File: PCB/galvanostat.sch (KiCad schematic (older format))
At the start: 27 parts, among them J0 Conn_01x02, J1 Conn_01x02, J2 Conn_01x02, U1 L7815, U2 LM358, U3 LM358, U4 LMC7660, U5 INA105KP, U6 LM358

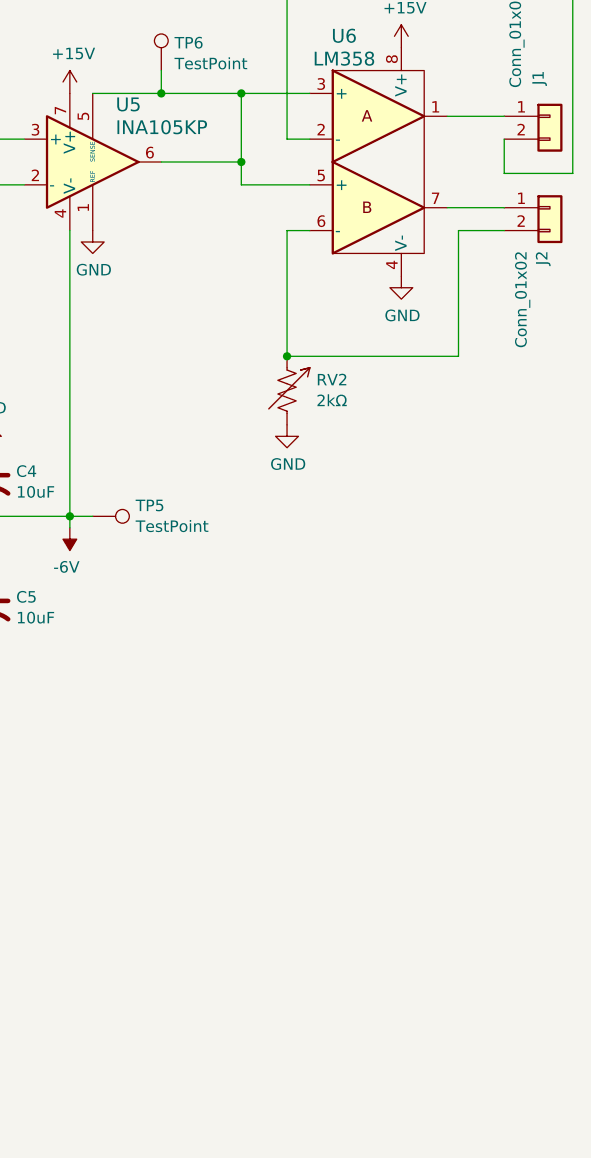
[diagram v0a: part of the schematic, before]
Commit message: dual to quad
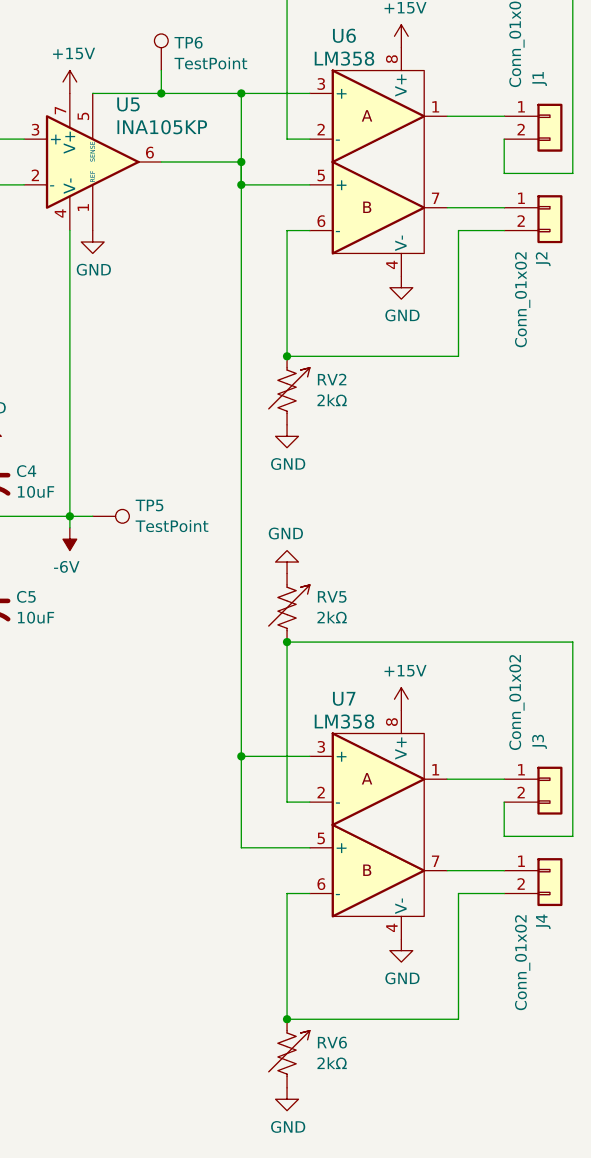
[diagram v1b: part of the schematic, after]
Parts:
- added J3, J4: Conn_01x02, Connector_Molex:Molex_KK-254_AE-6410-02A_1x02_P2.54mm_Vertical, symbol Connector_Generic:Conn_01x02
- added RV5, RV6: 2kΩ, Potentiometer_THT:Potentiometer_Bourns_3299W_Vertical, symbol Device:R_Variable_US
- added U7: LM358, Package_DIP:DIP-8_W7.62mm_Socket_LongPads, symbol LM358:LM358
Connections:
- net +15V: now also U7.8 (V+)
- net GND: now also RV5.1, RV6.2, U7.4 (V-)
- net at TP6.1, U5.5 (SENSE), U5.6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: now also U7.3 (+), U7.5 (+)
- new net: J3.1 (Pin_1), U7.1
- new net: J3.2 (Pin_2), RV5.2, U7.2 (-)
- new net: J4.1 (Pin_1), U7.7
- new net: J4.2 (Pin_2), RV6.1, U7.6 (-)
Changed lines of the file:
@@
 EESchema Schematic File Version 4
 LIBS:galvanostat-cache
-EELAYER 26 0
+EELAYER 29 0
 EELAYER END
 $Descr USLetter 11000 8500
 encoding utf-8
 Sheet 1 1
-Title "Dual Galvanostat"
-Date "2018-11-14"
-Rev "B"
+Title "Galvanostat"
+Date "2019-06-11"
+Rev "C"
 Comp ""
 Comment1 ""
@@
 Entry Wire Line
 	2700 3950 2800 4050
+$Comp
+L Connector_Generic:Conn_01x02 J3
+U 1 1 5D00B8A6
+P 9050 5150
+F 0 "J3" V 9000 5350 50  0000 R CNN
+F 1 "Conn_01x02" V 8900 5700 50  0000 R CNN
+F 2 "Connector_Molex:Molex_KK-254_AE-6410-02A_1x02_P2.54mm_Vertical" H 9050 5150 50  0001 C CNN
+F 3 "" H 9050 5150 50  0001 C CNN
+	1    9050 5150
+	1    0    0    -1
+$EndComp
+$Comp
+L power:+15V #PWR03
+U 1 1 5D00B8AC
+P 8400 4850
+F 0 "#PWR03" H 8400 4700 50  0001 C CNN
+F 1 "+15V" H 8415 5023 50  0000 C CNN
+F 2 "" H 8400 4850 50  0001 C CNN
+F 3 "" H 8400 4850 50  0001 C CNN
+	1    8400 4850
+	1    0    0    -1
+$EndComp
+$Comp
+L power:GND #PWR01
+U 1 1 5D00B8B2
+P 7900 4250
+F 0 "#PWR01" H 7900 4000 50  0001 C CNN
+F 1 "GND" H 7905 4077 50  0000 C CNN
+F 2 "" H 7900 4250 50  0001 C CNN
+F 3 "" H 7900 4250 50  0001 C CNN
+	1    7900 4250
+	-1   0    0    1
+$EndComp
+$Comp
+L Connector_Generic:Conn_01x02 J4
+U 1 1 5D00B8B8
+P 9050 5550
+F 0 "J4" V 9016 5362 50  0000 R CNN
+F 1 "Conn_01x02" V 8925 5362 50  0000 R CNN
+F 2 "Connector_Molex:Molex_KK-254_AE-6410-02A_1x02_P2.54mm_Vertical" H 9050 5550 50  0001 C CNN
+F 3 "" H 9050 5550 50  0001 C CNN
+	1    9050 5550
+	1    0    0    -1
+$EndComp
+$Comp
+L LM358:LM358 U7
+U 1 1 5D00B8BE
+P 8000 5350
+F 0 "U7" H 8150 5900 60  0000 C CNN
+F 1 "LM358" H 8150 5800 60  0000 C CNN
+F 2 "Package_DIP:DIP-8_W7.62mm_Socket_LongPads" H 8150 4900 60  0001 C CNN
+F 3 "" H 8000 5350 60  0000 C CNN
+	1    8000 5350
+	1    0    0    -1
+$EndComp
+$Comp
+L power:GND #PWR04
+U 1 1 5D00B8C4
+P 8400 5850
+F 0 "#PWR04" H 8400 5600 50  0001 C CNN
+F 1 "GND" H 8405 5677 50  0000 C CNN
+F 2 "" H 8400 5850 50  0001 C CNN
+F 3 "" H 8400 5850 50  0001 C CNN
+	1    8400 5850
+	1    0    0    -1
+$EndComp
+Wire Wire Line
+	8000 5250 7900 5250
+Wire Wire Line
+	8600 5550 8850 5550
+Wire Wire Line
+	8850 5650 8650 5650
+Wire Wire Line
+	8650 5650 8650 6200
+Wire Wire Line
+	8650 6200 7900 6200
+Wire Wire Line
+	7900 6200 7900 5650
+Wire Wire Line
+	7900 5650 8000 5650
+Wire Wire Line
+	8850 5250 8850 5400
+Wire Wire Line
+	8850 5400 9150 5400
+Wire Wire Line
+	8600 5150 8850 5150
+$Comp
+L power:GND #PWR02
+U 1 1 5D00B8D4
+P 7900 6500
+F 0 "#PWR02" H 7900 6250 50  0001 C CNN
+F 1 "GND" H 7905 6327 50  0000 C CNN
+F 2 "" H 7900 6500 50  0001 C CNN
+F 3 "" H 7900 6500 50  0001 C CNN
+	1    7900 6500
+	1    0    0    -1
+$EndComp
+Wire Wire Line
+	7700 5050 8000 5050
+Wire Wire Line
+	7700 5450 8000 5450
+$Comp
+L Device:R_Variable_US RV6
+U 1 1 5D00B8DC
+P 7900 6350
+F 0 "RV6" H 8028 6396 50  0000 L CNN
+F 1 "2kΩ" H 8028 6305 50  0000 L CNN
+F 2 "Potentiometer_THT:Potentiometer_Bourns_3299W_Vertical" V 7830 6350 50  0001 C CNN
+F 3 "" H 7900 6350 50  0001 C CNN
+	1    7900 6350
+	1    0    0    -1
+$EndComp
+Connection ~ 7900 6200
+$Comp
+L Device:R_Variable_US RV5
+U 1 1 5D00B8E3
+P 7900 4400
+F 0 "RV5" H 8028 4446 50  0000 L CNN
+F 1 "2kΩ" H 8028 4355 50  0000 L CNN
+F 2 "Potentiometer_THT:Potentiometer_Bourns_3299W_Vertical" V 7830 4400 50  0001 C CNN
+F 3 "" H 7900 4400 50  0001 C CNN
+	1    7900 4400
+	1    0    0    -1
+$EndComp
+Wire Wire Line
+	9150 4550 7900 4550
+Wire Wire Line
+	9150 4550 9150 5400
+Wire Wire Line
+	7900 4550 7900 5250
+Connection ~ 7900 4550
+Wire Wire Line
+	7700 5450 7700 5050
+Connection ~ 7700 2550
+Wire Wire Line
+	7700 2550 7700 2450
+Connection ~ 7700 5050
+Wire Wire Line
+	7700 5050 7700 2550
 $EndSCHEMATC

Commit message: revision C
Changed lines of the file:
@@
 	5200 2150 5550 2150
 Connection ~ 4700 2550
-Entry Wire Line
-	2700 3950 2800 4050
 $Comp
 L Connector_Generic:Conn_01x02 J3
@@
 	7700 5450 7700 5050
 Connection ~ 7700 2550
-Wire Wire Line
-	7700 2550 7700 2450
 Connection ~ 7700 5050
 Wire Wire Line
